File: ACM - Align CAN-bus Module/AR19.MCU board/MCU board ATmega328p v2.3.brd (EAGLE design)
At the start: 25.4 x 39 mm, 44 parts, among them IC1 ATMEGA328P-MMH, IC2 MIC5239-5.0YS_TR, IC3 MCP25625-E_ML, J1 AVR_SPI_PROG_3X2NS

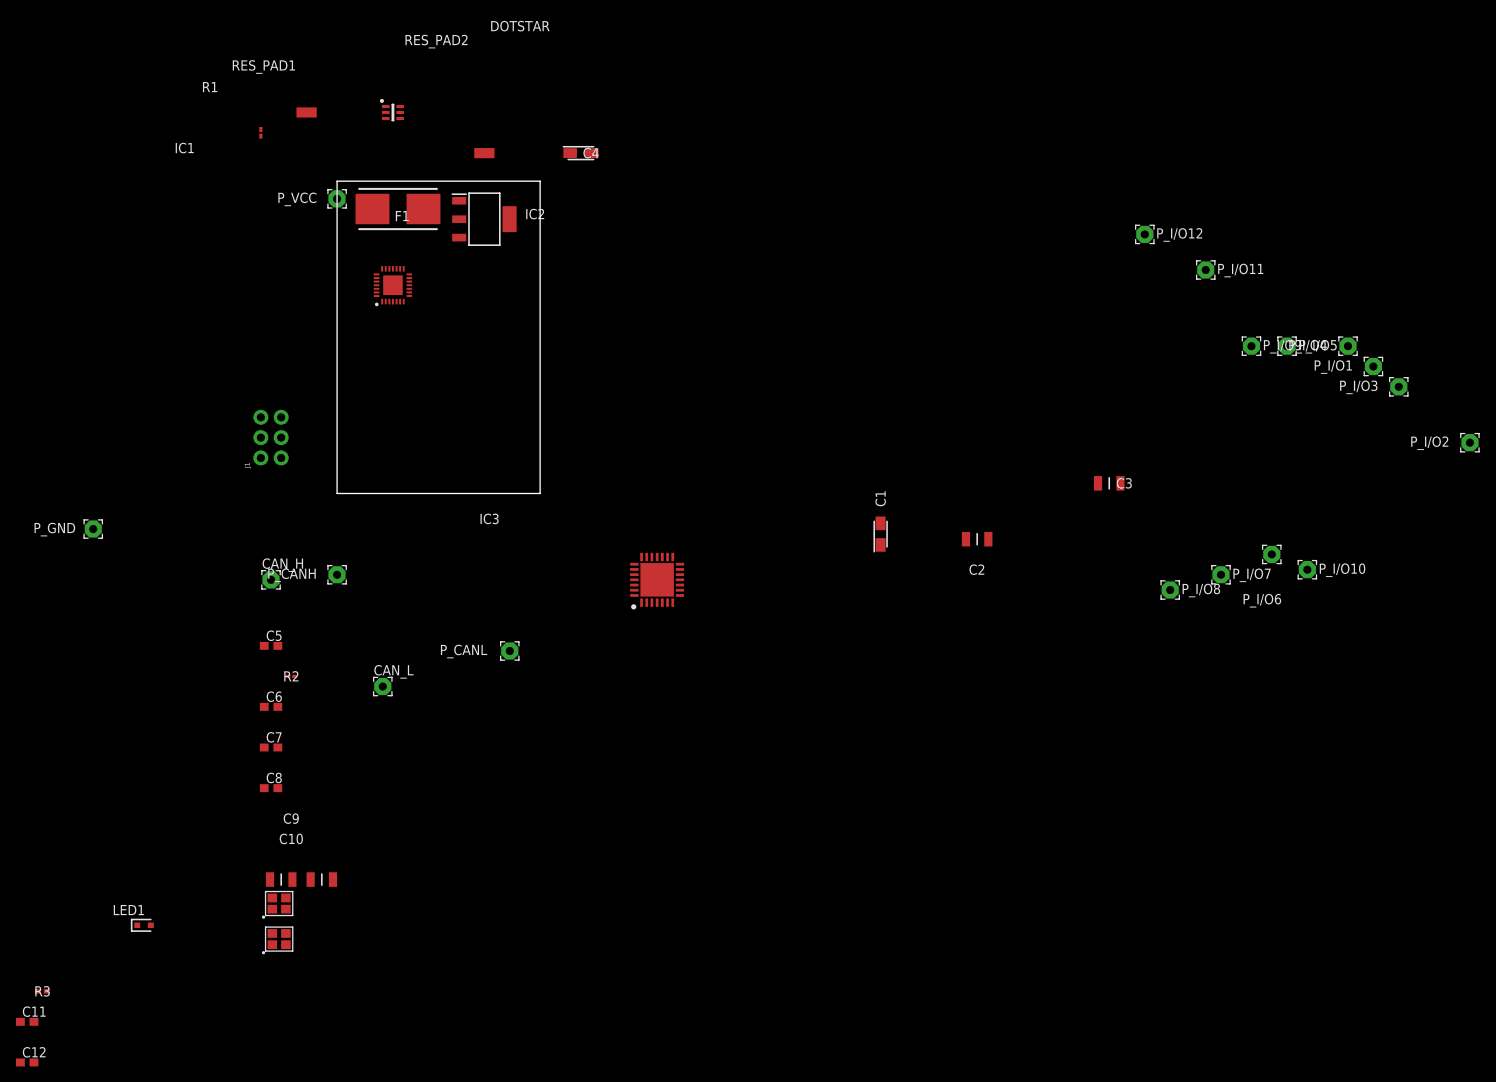
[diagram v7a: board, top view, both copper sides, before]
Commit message: Removed: Extra CAN port and Tested Board routing
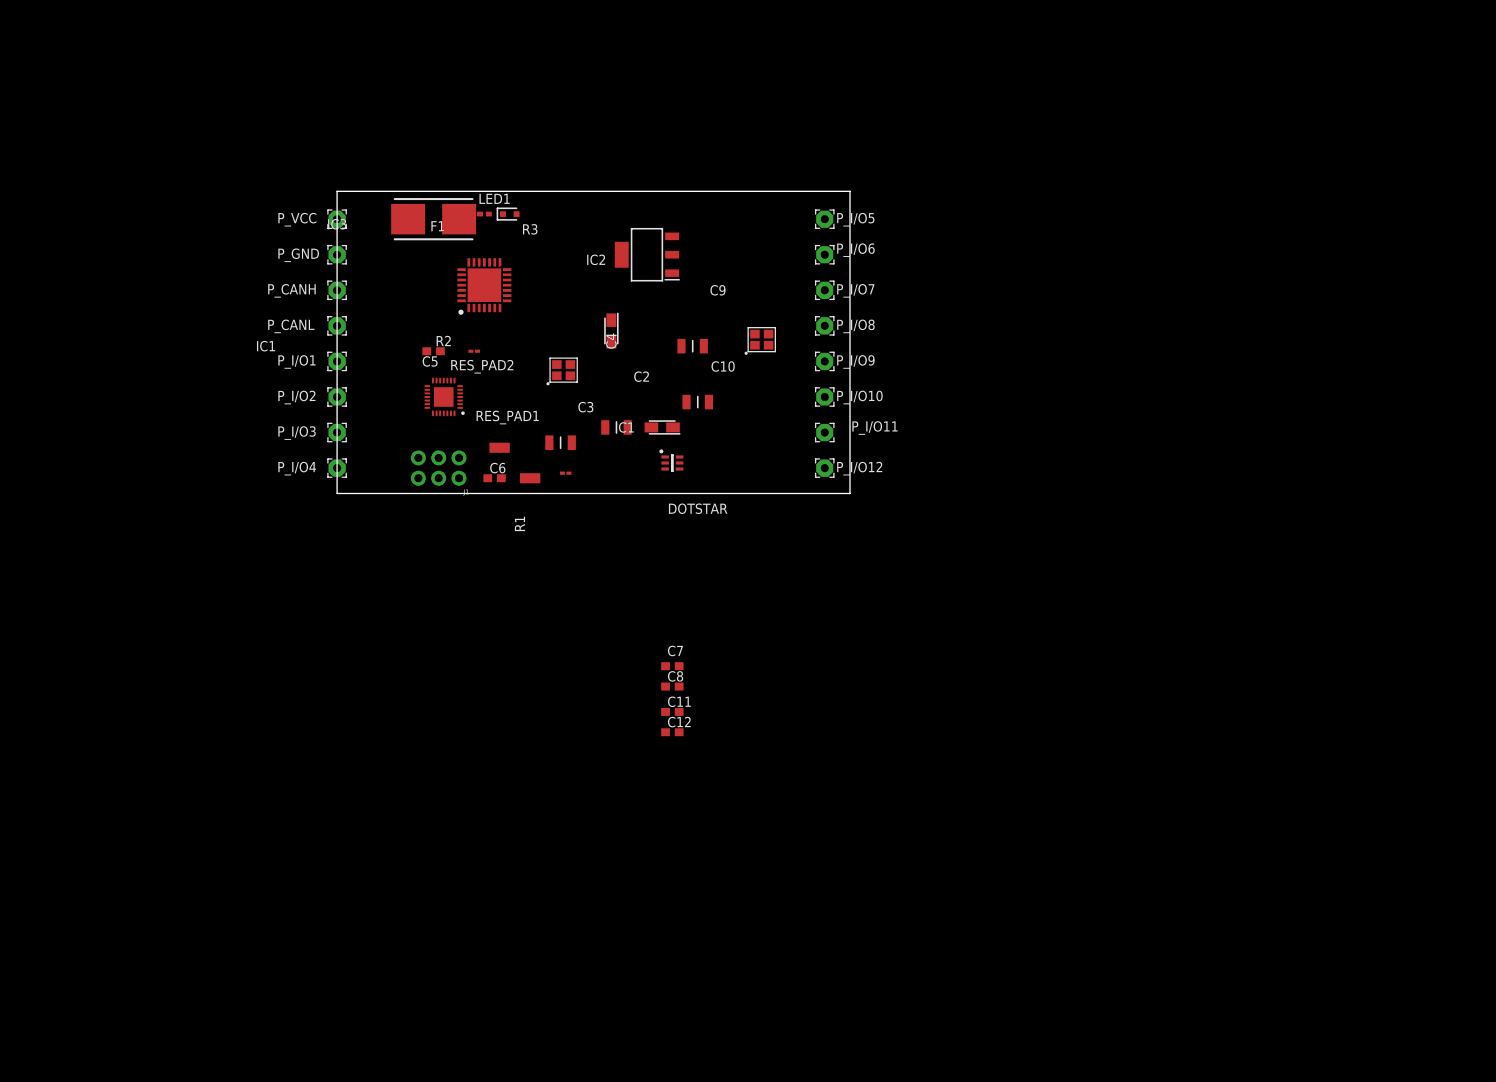
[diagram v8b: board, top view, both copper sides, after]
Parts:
- removed CAN_H, CAN_L: (no value), wirepad:2,15/1,0
- moved P_I/O2 141.7 mm to (0.00, 12.1)
- moved P_I/O3 132.8 mm to (0.00, 7.62)
- moved P_I/O1 129.5 mm to (0.00, 16.5)
- moved P_I/O4 127.3 mm to (0.00, 3.17)
- moved R3 111.8 mm to (18.4, 34.9), turned to 180 degrees
- moved LED1 100.0 mm to (21.6, 34.9)
- moved U$1 92.8 mm to (51.4, 17.8)
- moved C12 90.6 mm to (41.9, -29.8)
- moved C11 89.5 mm to (41.9, -27.3)
- moved C9 84.2 mm to (44.5, 18.4)
- moved U$2 79.5 mm to (26.7, 14.0)
- moved C10 76.0 mm to (45.1, 11.4)
- moved C3 68.8 mm to (27.9, 6.35)
- moved P_I/O6 67.3 mm to (61.0, 29.8)
- moved P_I/O10 64.1 mm to (61.0, 12.1)
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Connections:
- net CANH: no longer CAN_H.1
- net CANL: no longer CAN_L.1
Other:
- board size 25.4 x 39 mm -> 64.1 x 37.8 mm
